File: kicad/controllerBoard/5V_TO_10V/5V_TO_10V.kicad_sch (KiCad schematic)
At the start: 51 parts, among them Q635 Q_PMOS_GSD, Q636 Q_PMOS_GSD, Q637 Q_NMOS_GSD, Q638 Q_NMOS_GSD, Q639 Q_PMOS_GSD, Q640 Q_NMOS_GSD, Q641 Q_PMOS_GSD, Q642 Q_NMOS_GSD, Q643 Q_PMOS_GSD, Q644 Q_NMOS_GSD, Q645 Q_PMOS_GSD, Q646 Q_NMOS_GSD, Q647 Q_PMOS_GSD, Q648 Q_NMOS_GSD, Q649 Q_PMOS_GSD, Q650 Q_NMOS_GSD, Q651 Q_PMOS_GSD, Q652 Q_NMOS_GSD

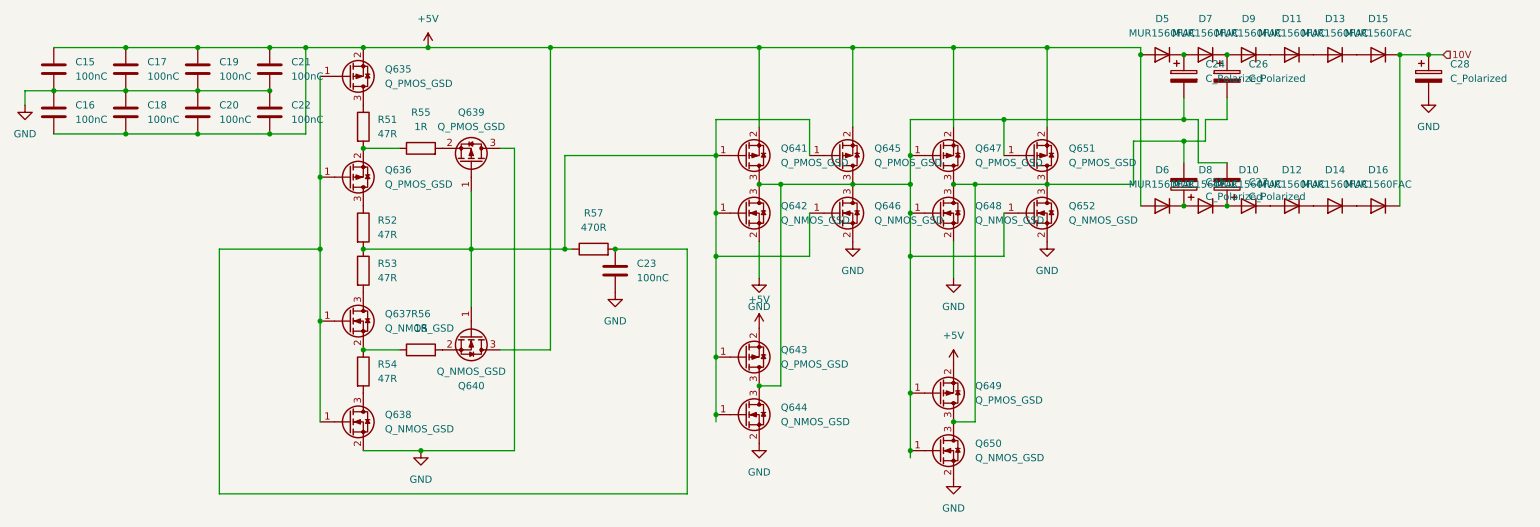
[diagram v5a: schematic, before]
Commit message: update bom, add more capacitors
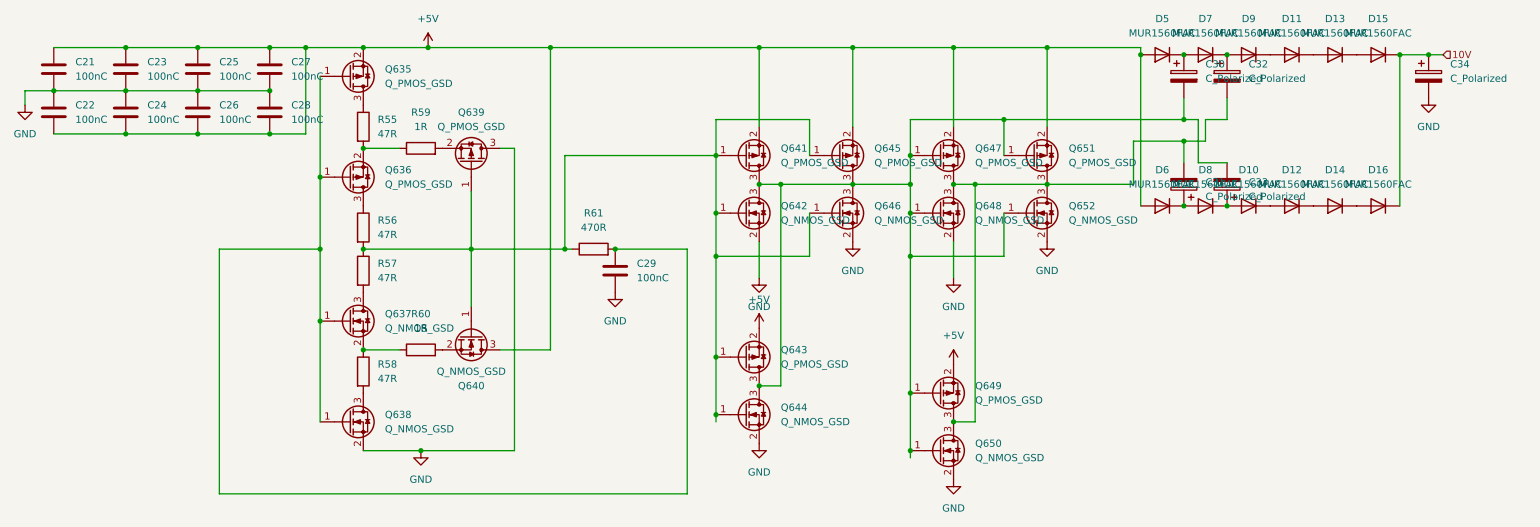
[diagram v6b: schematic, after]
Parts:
- renumbered C15 to C21, C16 to C22, C17 to C23, C18 to C24, C19 to C25, C20 to C26, C21 to C27, C22 to C28, C23 to C29, C24 to C30, C25 to C31, C26 to C32, C27 to C33, C28 to C34, R51 to R55, R52 to R56, R53 to R57, R54 to R58, R55 to R59, R56 to R60, R57 to R61
